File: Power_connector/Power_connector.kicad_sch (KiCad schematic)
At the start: 33 parts, among them J1 XT60_F, J10 XT60_F, J11 XT60_F, J12 XT60_F, J2 XT60_Male, J3 XT60_F, J4 XT60_F, J5 Screw_Terminal_01x02, J6 XT60_F, J7 XT60_F, J8 XT60_F, J9 XT60_F, Q1 IRFS7530, Q2 IRFS7530, Q3 IRFS7530

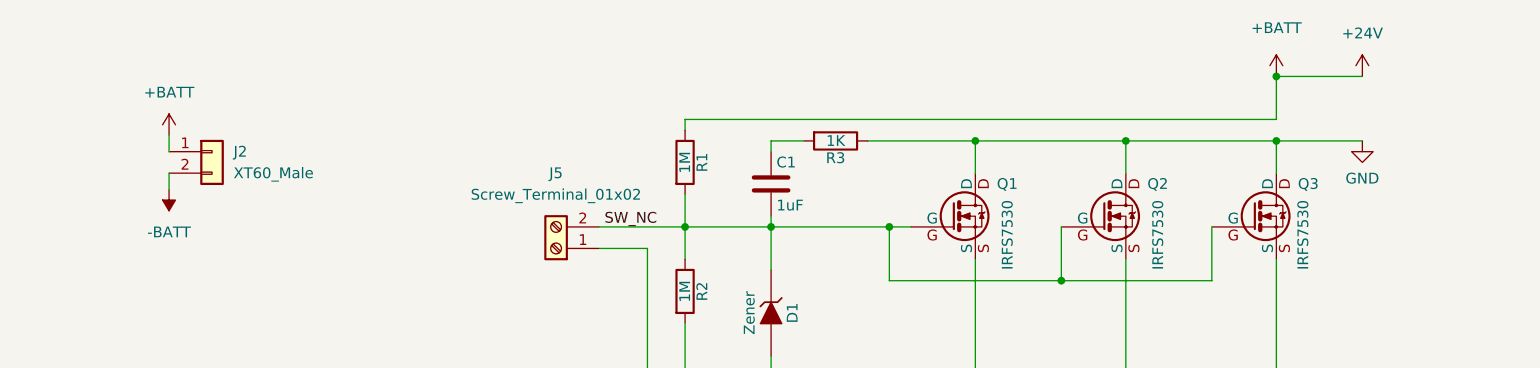
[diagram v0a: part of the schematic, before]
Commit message: added power board
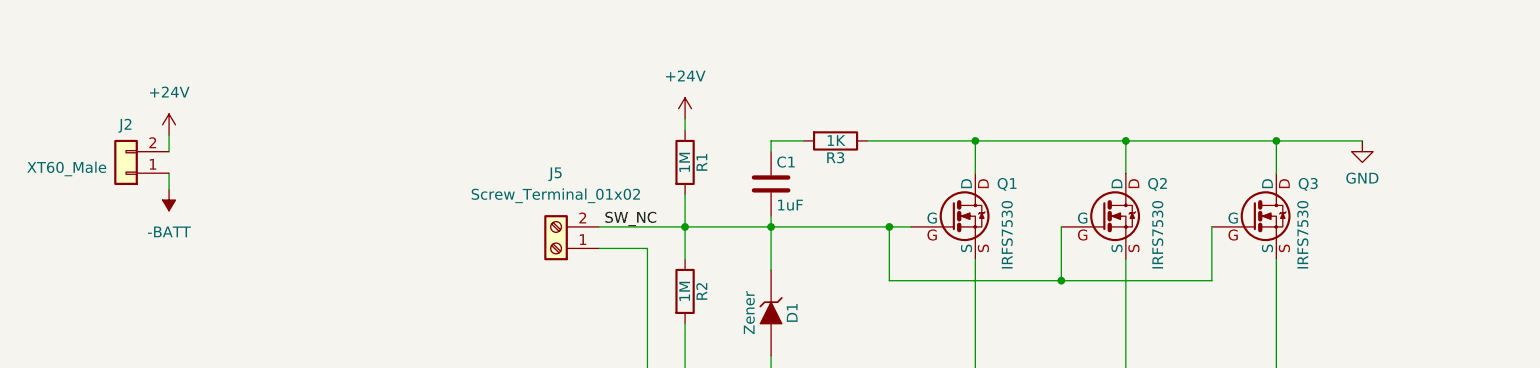
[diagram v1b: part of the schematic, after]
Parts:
- F1, F10, F2, F3, F4, F5, F6, F7, F8, F9: footprint (none) -> PolyuRobotics:FUSE_3557-2
- Q1, Q2, Q3: footprint (none) -> sparkparts:D2PAK-7-GDS
- R1, R2, R3: footprint (none) -> Resistor_SMD:R_0805_2012Metric_Pad1.20x1.40mm_HandSolder
- R4, R5: footprint (none) -> Resistor_SMD:R_1206_3216Metric_Pad1.30x1.75mm_HandSolder
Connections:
- net +24V: now also J2.2 (Pin_2); no longer J2.1 (Pin_1)
- net -BATT: now also J2.1 (Pin_1); no longer J2.2 (Pin_2)
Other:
- moved on the sheet: J2

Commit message: power board
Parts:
- added D10, D11, D12, D13, D3, D4, D5, D6, D7, D8, D9: 1N4001, Diode_THT:D_DO-41_SOD81_P10.16mm_Horizontal, symbol Diode:1N4001
- added D2: (no value), symbol Diode:1N4001
- added F11, F12: 3557-2, PolyuRobotics:FUSE_3557-2, symbol Device:Fuse_Small
- added J13, J14: XT60_F, Connector_AMASS:AMASS_XT60-F_1x02_P7.20mm_Vertical, symbol Connector_Generic:Conn_01x02
- added Q4: IRFS7530, sparkparts:D2PAK-7-GDS, symbol sparkparts:IRFS7530
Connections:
- net +24V: now also D10.1 (K), D11.1 (K), D12.1 (K), D13.1 (K), D2.1 (K), D3.1 (K), D4.1 (K), D5.1 (K), D6.1 (K), D7.1 (K), D8.1 (K), D9.1 (K), F11.2, F12.2
- net -BATT: now also Q4.S
- net GND: now also D10.2 (A), D11.2 (A), D12.2 (A), D13.2 (A), D2.2 (A), D3.2 (A), D4.2 (A), D5.2 (A), D6.2 (A), D7.2 (A), D8.2 (A), D9.2 (A), J13.2 (Pin_2), J14.2 (Pin_2), Q4.D
- net SW_NC: now also Q4.G
- new net: F12.1, J14.1 (Pin_1)
- new net: F11.1, J13.1 (Pin_1)
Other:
- moved on the sheet: J2, LED1, R4, R5

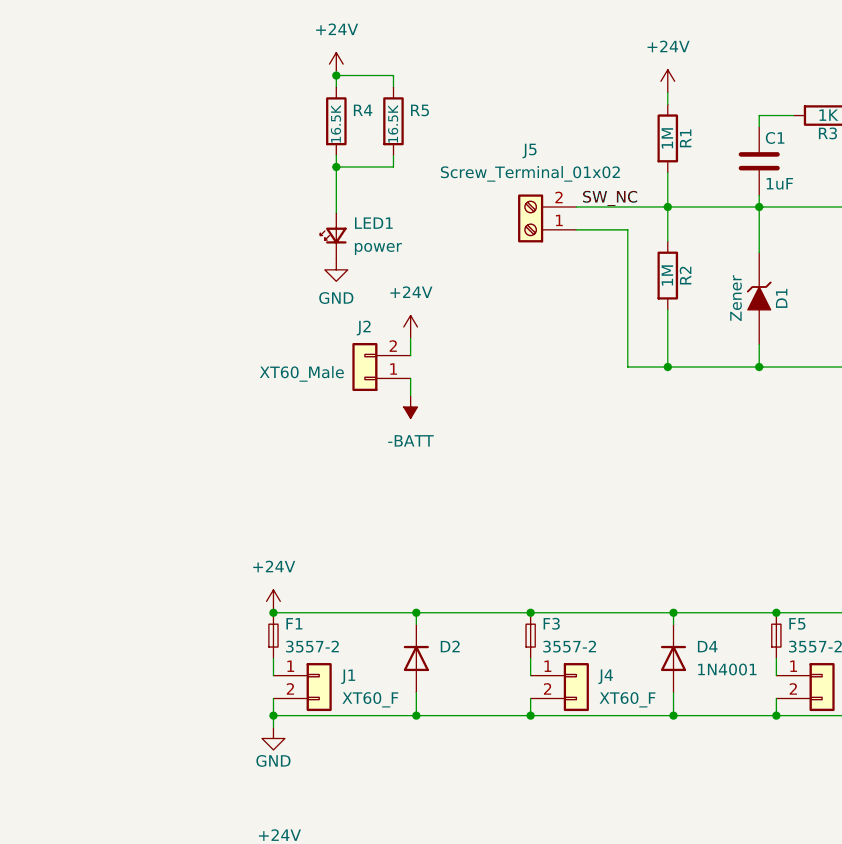
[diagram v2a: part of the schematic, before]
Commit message: power connector added
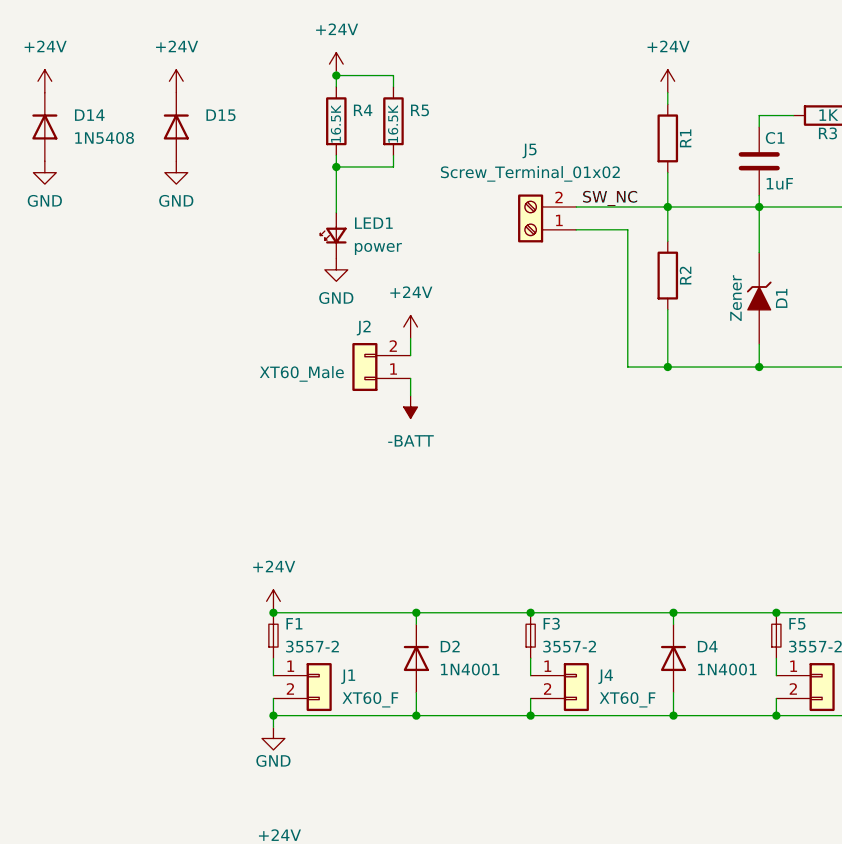
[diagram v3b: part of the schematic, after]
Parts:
- added D14: 1N5408, Diode_THT:D_DO-201AD_P15.24mm_Horizontal, symbol Diode:1N5408
- added D15: (no value), symbol Diode:1N5408
- D2: value (none) -> 1N4001; footprint (none) -> Diode_THT:D_DO-41_SOD81_P10.16mm_Horizontal
- R1, R2: value 1M -> (none)
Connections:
- net +24V: now also D14.1 (K), D15.1 (K)
- net GND: now also D14.2 (A), D15.2 (A)
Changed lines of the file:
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@@
     (in_bom yes) (on_board yes)
     (property "Reference" "R2" (id 0) (at 99.187 66.675 90))
-    (property "Value" "1M" (id 1) (at 97.155 66.675 90))
+    (property "Value" "" (id 1) (at 97.155 66.675 90))
     (property "Footprint" "Resistor_SMD:R_0805_2012Metric_Pad1.20x1.40mm_HandSolder" (id 2) (at 95.377 66.675 90)
       (effects (font (size 1.27 1.27)) hide)
@@
     (in_bom yes) (on_board yes)
     (property "Reference" "R1" (id 0) (at 99.187 51.435 90))
-    (property "Value" "1M" (id 1) (at 97.155 51.435 90))
+    (property "Value" "" (id 1) (at 97.155 51.435 90))
     (property "Footprint" "Resistor_SMD:R_0805_2012Metric_Pad1.20x1.40mm_HandSolder" (id 2) (at 95.377 51.435 90)
       (effects (font (size 1.27 1.27)) hide)
@@
     (pin "2")
   )
+  (symbol (lib_id "power:GND") (at 27.94 53.975 0) (unit 1)
+    (in_bom yes) (on_board yes) (fields_autoplaced)
+    (property "Reference" "#PWR0115" (id 0) (at 27.94 60.325 0)
+      (effects (font (size 1.27 1.27)) hide)
+    )
+    (property "Value" "GND" (id 1) (at 27.94 58.42 0))
+    (property "Footprint" "" (id 2) (at 27.94 53.975 0)
+      (effects (font (size 1.27 1.27)) hide)
+    )
+    (property "Datasheet" "" (id 3) (at 27.94 53.975 0)
+      (effects (font (size 1.27 1.27)) hide)
+    )
+    (pin "1")
+  )
   (symbol (lib_id "power:+24V") (at 60.325 44.45 0) (unit 1)
     (in_bom yes) (on_board yes) (fields_autoplaced)
@@
       (effects (font (size 1.27 1.27)) (justify left))
     )
-    (property "Value" "" (id 1) (at 71.755 110.4899 90)
-      (effects (font (size 1.27 1.27)) (justify left))
-    )
-    (property "Footprint" "" (id 2) (at 64.77 109.22 0)
+    (property "Value" "1N4001" (id 1) (at 71.755 110.4899 90)
+      (effects (font (size 1.27 1.27)) (justify left))
+    )
+    (property "Footprint" "Diode_THT:D_DO-41_SOD81_P10.16mm_Horizontal" (id 2) (at 64.77 109.22 0)
       (effects (font (size 1.27 1.27)) hide)
     )
@@
     )
     (property "Datasheet" "~" (id 3) (at 53.34 106.68 0)
+      (effects (font (size 1.27 1.27)) hide)
+    )
+    (pin "1")
+    (pin "2")
+  )
+  (symbol (lib_id "Diode:1N5408") (at 42.545 50.165 270) (unit 1)
+    (in_bom yes) (on_board yes) (fields_autoplaced)
+    (property "Reference" "D15" (id 0) (at 45.72 48.8949 90)
+      (effects (font (size 1.27 1.27)) (justify left))
+    )
+    (property "Value" "" (id 1) (at 45.72 51.4349 90)
+      (effects (font (size 1.27 1.27)) (justify left))
+    )
+    (property "Footprint" "" (id 2) (at 38.1 50.165 0)
+      (effects (font (size 1.27 1.27)) hide)
+    )
+    (property "Datasheet" "http://www.vishay.com/docs/88516/1n5400.pdf" (id 3) (at 42.545 50.165 0)
       (effects (font (size 1.27 1.27)) hide)
     )
@@
     (pin "1")
     (pin "2")
+  )
+  (symbol (lib_id "power:GND") (at 42.545 53.975 0) (unit 1)
+    (in_bom yes) (on_board yes) (fields_autoplaced)
+    (property "Reference" "#PWR0112" (id 0) (at 42.545 60.325 0)
+      (effects (font (size 1.27 1.27)) hide)
+    )
+    (property "Value" "GND" (id 1) (at 42.545 58.42 0))
+    (property "Footprint" "" (id 2) (at 42.545 53.975 0)
+      (effects (font (size 1.27 1.27)) hide)
+    )
+    (property "Datasheet" "" (id 3) (at 42.545 53.975 0)
+      (effects (font (size 1.27 1.27)) hide)
+    )
+    (pin "1")
   )
   (symbol (lib_id "Diode:1N4001") (at 69.85 139.065 270) (unit 1)
@@
     (pin "S")
   )
+  (symbol (lib_id "power:+24V") (at 42.545 46.355 0) (unit 1)
+    (in_bom yes) (on_board yes) (fields_autoplaced)
+    (property "Reference" "#PWR0113" (id 0) (at 42.545 50.165 0)
+      (effects (font (size 1.27 1.27)) hide)
+    )
+    (property "Value" "+24V" (id 1) (at 42.545 41.275 0))
+    (property "Footprint" "" (id 2) (at 42.545 46.355 0)
+      (effects (font (size 1.27 1.27)) hide)
+    )
+    (property "Datasheet" "" (id 3) (at 42.545 46.355 0)
+      (effects (font (size 1.27 1.27)) hide)
+    )
+    (pin "1")
+  )
   (symbol (lib_id "Device:Fuse_Small") (at 53.975 136.525 90) (unit 1)
     (in_bom yes) (on_board yes) (fields_autoplaced)
@@
     (pin "2")
   )
+  (symbol (lib_id "Diode:1N5408") (at 27.94 50.165 270) (unit 1)
+    (in_bom yes) (on_board yes) (fields_autoplaced)
+    (property "Reference" "D14" (id 0) (at 31.115 48.8949 90)
+      (effects (font (size 1.27 1.27)) (justify left))
+    )
+    (property "Value" "1N5408" (id 1) (at 31.115 51.4349 90)
+      (effects (font (size 1.27 1.27)) (justify left))
+    )
+    (property "Footprint" "Diode_THT:D_DO-201AD_P15.24mm_Horizontal" (id 2) (at 23.495 50.165 0)
+      (effects (font (size 1.27 1.27)) hide)
+    )
+    (property "Datasheet" "http://www.vishay.com/docs/88516/1n5400.pdf" (id 3) (at 27.94 50.165 0)
+      (effects (font (size 1.27 1.27)) hide)
+    )
+    (pin "1")
+    (pin "2")
+  )
   (symbol (lib_id "Device:Fuse_Small") (at 193.675 136.525 90) (unit 1)
     (in_bom yes) (on_board yes) (fields_autoplaced)
@@
     (pin "1")
     (pin "2")
+  )
+  (symbol (lib_id "power:+24V") (at 27.94 46.355 0) (unit 1)
+    (in_bom yes) (on_board yes) (fields_autoplaced)
+    (property "Reference" "#PWR0114" (id 0) (at 27.94 50.165 0)
+      (effects (font (size 1.27 1.27)) hide)
+    )
+    (property "Value" "+24V" (id 1) (at 27.94 41.275 0))
+    (property "Footprint" "" (id 2) (at 27.94 46.355 0)
+      (effects (font (size 1.27 1.27)) hide)
+    )
+    (property "Datasheet" "" (id 3) (at 27.94 46.355 0)
+      (effects (font (size 1.27 1.27)) hide)
+    )
+    (pin "1")
   )
   (symbol (lib_id "Connector_Generic:Conn_01x02") (at 59.055 140.97 0) (unit 1)
@@
       (reference "#PWR0111") (unit 1) (value "GND") (footprint "")
     )
+    (path "/48025395-42dd-4d12-ad73-507ffc428ed2"
+      (reference "#PWR0112") (unit 1) (value "GND") (footprint "")
+    )
+    (path "/5bddf81b-04a7-43e1-8857-2461efbac6ab"
+      (reference "#PWR0113") (unit 1) (value "+24V") (footprint "")
+    )
+    (path "/8141875e-5111-4a29-816a-e7f55286ccb6"
+      (reference "#PWR0114") (unit 1) (value "+24V") (footprint "")
+    )
+    (path "/29779332-69a9-4411-a3b9-d8914d52a0c5"
+      (reference "#PWR0115") (unit 1) (value "GND") (footprint "")
+    )
     (path "/00000000-0000-0000-0000-00005775e442"
       (reference "C1") (unit 1) (value "1uF") (footprint "Capacitor_SMD:C_0805_2012Metric_Pad1.18x1.45mm_HandSolder")
@@
       (reference "D13") (unit 1) (value "1N4001") (footprint "Diode_THT:D_DO-41_SOD81_P10.16mm_Horizontal")
     )
+    (path "/6832f67c-23e3-4f71-ab10-4010d49a3fbc"
+      (reference "D14") (unit 1) (value "1N5408") (footprint "Diode_THT:D_DO-201AD_P15.24mm_Horizontal")
+    )
+    (path "/3a6ee388-892e-49d3-9fe3-501adb26cb08"
+      (reference "D15") (unit 1) (value "1N5408") (footprint "Diode_THT:D_DO-201AD_P15.24mm_Horizontal")
+    )
     (path "/3806654f-70ad-4eea-b682-a6d648524051"
       (reference "F1") (unit 1) (value "3557-2") (footprint "PolyuRobotics:FUSE_3557-2")
@@
     )
     (path "/00000000-0000-0000-0000-00005775e3d7"
-      (reference "R1") (unit 1) (value "1M") (footprint "Resistor_SMD:R_0805_2012Metric_Pad1.20x1.40mm_HandSolder")
+      (reference "R1") (unit 1) (value "1.5M") (footprint "Resistor_SMD:R_0805_2012Metric_Pad1.20x1.40mm_HandSolder")
     )
     (path "/00000000-0000-0000-0000-00005775e315"
-      (reference "R2") (unit 1) (value "1M") (footprint "Resistor_SMD:R_0805_2012Metric_Pad1.20x1.40mm_HandSolder")
+      (reference "R2") (unit 1) (value "400k") (footprint "Resistor_SMD:R_0805_2012Metric_Pad1.20x1.40mm_HandSolder")
     )
     (path "/00000000-0000-0000-0000-00005775e416"

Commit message: powerboard mod
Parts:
- removed D10, D11, D12, D13, D2, D3, D4, D5, D6, D7, D8, D9: 1N4001, Diode_THT:D_DO-41_SOD81_P10.16mm_Horizontal, symbol Diode:1N4001
- removed F2, F4, F6: 3557-2, PolyuRobotics:FUSE_3557-2, symbol Device:Fuse_Small
- removed J3, J6, J8: XT60_F, Connector_AMASS:AMASS_XT60-F_1x02_P7.20mm_Vertical, symbol Connector_Generic:Conn_01x02
- removed Q1, Q2: IRFS7530, sparkparts:D2PAK-7-GDS, symbol sparkparts:IRFS7530
- added D10, D11, D12, D13, D14, D15, D3, D5, D7, D8, D9: indicator, symbol Device:LED_Small
- added D4: (no value), symbol Device:LED_Small
- added F11, F7, F9: 3557-2, PolyuRobotics:FUSE_3557-2, symbol Device:Fuse_Small
- added J11, J13, J9: XT60_F, Connector_AMASS:AMASS_XT60-F_1x02_P7.20mm_Vertical, symbol Connector_Generic:Conn_01x02
- added LED1: BATT, LED_SMD:LED_0805_2012Metric_Pad1.15x1.40mm_HandSolder, symbol Device:LED_Small
- added R1: 10M, Resistor_SMD:R_0805_2012Metric, symbol Device:R_Small
- added R10, R11, R12, R13, R14, R15, R16, R17, R18, R2, R6: 10M, symbol Device:R_Small
- added R4: (no value), symbol Device:R_Small
- D2: renamed from D15; value (none) -> 1N5408; footprint (none) -> Diode_THT:D_DO-201AD_P15.24mm_Horizontal
- J4: renamed from J5; value Screw_Terminal_01x02 -> E_Stop
- R7: renamed from R1; value (none) -> 1.5M
- R8: renamed from R2; value (none) -> 400k
- renumbered D14 to D1, D1 to D6, F3 to F2, F5 to F3, F7 to F4, F9 to F5, F11 to F6, J4 to J3, J7 to J5, J9 to J6, J11 to J7, J13 to J8, LED1 to LED2, Q3 to Q1, Q4 to Q2, R4 to R3, R3 to R9
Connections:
- net +24V: now also D6.2 (A), J4.1 (Pin_1), Q1.S, Q2.S, R8.2, F11.2, F7.2, F9.2; no longer J2.2 (Pin_2), R7.1
- net GND: now also J1.1 (Pin_1), J10.1 (Pin_1), J12.1 (Pin_1), J14.1 (Pin_1), J2.1 (Pin_1), J3.1 (Pin_1), J5.1 (Pin_1), J6.1 (Pin_1), J7.1 (Pin_1), J8.1 (Pin_1), D10.1 (K), D11.1 (K), D13.1 (K), D14.1 (K), D15.1 (K), D3.1 (K), D4.1 (K), D7.1 (K), D8.1 (K), D9.1 (K), J11.1 (Pin_1), J13.1 (Pin_1), J9.1 (Pin_1), LED1.1 (K); no longer J1.2 (Pin_2), J10.2 (Pin_2), J12.2 (Pin_2), J14.2 (Pin_2), J3.2 (Pin_2), J5.2 (Pin_2), J6.2 (Pin_2), J7.2 (Pin_2), J8.2 (Pin_2), Q1.D, Q2.D, R9.1
- net at F2.1: now also J3.2 (Pin_2), R4.1; no longer J3.1 (Pin_1)
- net at F10.1: now also J12.2 (Pin_2), R16.1; no longer J12.1 (Pin_1)
- net at F8.1: now also J10.2 (Pin_2), R14.1; no longer J10.1 (Pin_1)
- net at F4.1: now also J6.2 (Pin_2), R10.1; no longer J6.1 (Pin_1)
- net at F1.1: now also J1.2 (Pin_2), R2.1; no longer J1.1 (Pin_1)
- net at F5.1: now also J7.2 (Pin_2), R11.1; no longer J7.1 (Pin_1)
- net at F12.1: now also J14.2 (Pin_2), R18.1; no longer J14.1 (Pin_1)
- net at F6.1: now also J8.2 (Pin_2), R12.1; no longer J8.1 (Pin_1)
- net at F3.1: now also J5.2 (Pin_2), R6.1; no longer J5.1 (Pin_1)
- removed net -BATT: D6.2 (A), J2.1 (Pin_1), J4.1 (Pin_1), Q1.S, Q2.S, R8.2
- new net: LED1.2 (A), R1.2
- new net: D3.2 (A), R2.2
- new net: D7.2 (A), R10.2
- new net: D8.2 (A), R11.2
- new net: F7.1, J9.2 (Pin_2), R13.1
- new net: D13.2 (A), R16.2
- new net: D12.2 (A), R15.2
- new net: D10.2 (A), R13.2
- new net: D15.2 (A), R18.2
- new net: F9.1, J11.2 (Pin_2), R15.1
- new net: F11.1, J13.2 (Pin_2), R17.1
- new net: D4.2 (A), R4.2
- new net: D5.2 (A), R6.2
- new net: D9.2 (A), R12.2
- new net: D14.2 (A), R17.2
- new net: D11.2 (A), R14.2
- new net +BATT: J2.2 (Pin_2), Q1.D, Q2.D, R1.1, R7.1, R9.1
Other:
- moved on the sheet: C1, D1, D2, D6, F1, F2, F3, F4, F5, F6, J1, J2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
